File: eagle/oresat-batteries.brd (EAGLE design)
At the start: 99 x 95.3 mm, 107 parts, among them IC1 74AHC1G08DBV, J1 J-SAMTEC-TFM-120-X1-XXX-D-RA, J7 1.27MM-SWD-CONNECTOR, Q1 CSD16340Q3, Q10 TPN4R712MD, Q11 TPN4R712MD, Q12 TPN4R712MD, Q2 CSD16340Q3, Q3 TPN4R712MD, Q4 TPN4R712MD, Q5 TPN4R712MD, Q6 TPN4R712MD, Q8 TPN4R712MD, Q9 TPN4R712MD, U1 TPS63070, U10 LTC4412, U11 MAX17055, U12 LTC4412, U13 LTC4412, U2 TCAN330, U3 BQ2970, U4 LTC4411, U5 LTC4411, U6 STM32F042K6, U7 LTC4411, U8 LTC4411, U9 LTC4412, X1 16MHZ-2.5x2mm

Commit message: New 2S2P battery boards, based on 18650 cells along with a BQ28400 battery IC.
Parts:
- removed C11, C16: 20p, rcl_custom:.0402-B-NOSILK
- removed C14: 22u, oresat-rcl:.0603-B-NOSILK
- removed C17, C22: 100n, rcl_custom:.0402-B-NOSILK
- removed C18, C25: 22u, oresat-rcl:.0805-B-NOSILK
- removed D1, D2, D3: GREEN, SparkFun-LED:LED-0603
- removed F2: 2016L500DR, F-LITTELFUSE-2016L-SERIES-PTC:2016L
- removed H1, H2, H3, H4: STAND-OFFTIGHT, SparkFun-Hardware:STAND-OFF-TIGHT
- removed IC1: 74AHC1G08DBV, 74xx-little-us:SOT23-5
- removed J5: (no value), SparkFun-Connectors:6_PIN_SERIAL_TARGET_SIDE_W_SILK
- removed J7: 1.27MM-SWD-CONNECTOR, J-CNC-3220-10-0100-00-ARM-SWD-port:1.27MM_2X5
- removed JP8: (no value), pinhead:1X02
- removed L3: 1.5 uH, L-Coilcraft-XFL4020:L-COILCRAFT-XFL4020
- removed Q10, Q11, Q12, Q6, Q8, Q9: TPN4R712MD, tpn4r712md-pmosfet:TSON-ADVANCE-3X3
- removed R18: NP, rcl_custom:.0402-B-NOSILK
- removed R19, R21, R26, R28, R29: 10k, rcl:R0603
- removed R20: 4.19, oresat-batteries:RES_HEATER
- removed R22, R23, R24, R25: 470k, rcl:R0603
- removed R27: 3.3k, rcl:R0402
- removed R3: 2.7k, rcl_custom:.0402-B-NOSILK
- removed TP10, TP11, TP12, TP13, TP14, TP16, TP17, TP20, TP6, TP7, TP8, TP9: TP, oresat-batteries:2MM_TP
- removed TP15, TP4, TP5: TEST-POINT, Tova:2MM-TEST-POINT
- removed U$2: (no value), oresat-card:ORESAT-CARD-V1.0
- removed U10, U12, U13, U9: LTC4412, ltc4412:SOT23-6
- removed U11: MAX17055, max17055:TDFN-10L
- removed U2: TCAN330, TCAN330:SOT23-8_TI-DCN
- removed U3: BQ2970, oresat-batteries:PSOP6
- removed U4, U5, U7, U8: LTC4411, ltc4411:SOT23-5-B
- removed U6: STM32F042K6, STM32F042K:QFP32-7X7
- removed X1: 16MHZ-2.5x2mm, low-gain-radio:CRYSTAL_2.5X2
- added B2, B3, B4: B-18650-LI-BATTERY, B-18650-Li-battery:18650
- added TR1: 10k, oresat-rcl:.0603-B-NOSILK
- B1: value 2AHBATT -> B-18650-LI-BATTERY; device oresat-batteries:2AH_605060 -> B-18650-Li-battery:18650
- C1: value .1u -> 1u; device rcl:C0603 -> oresat-rcl:.0603-B-NOSILK
- C10, C7: value .1u -> 100n; device rcl:C0603 -> oresat-rcl:.0402-B-NOSILK
- C2: value .47u -> 100n; device rcl:C0603 -> oresat-rcl:.0402-B-NOSILK
- C3, C5, C9: device rcl_custom:.0402-B-NOSILK -> oresat-rcl:.0402-B-NOSILK
- C4: value 10u -> 100n; device oresat-rcl:.0603-B-NOSILK -> oresat-rcl:.0402-B-NOSILK
- C6: value 10u -> 1u; device oresat-rcl:.0805-B-NOSILK -> oresat-rcl:.0603-B-NOSILK
- C8: value 10u -> 100n; device oresat-rcl:.0805-B-NOSILK -> oresat-rcl:.0402-B-NOSILK
- Q1, Q2: value CSD16340Q3 -> MOSFET-PCH-SOT23-6; device oresat-batteries:Q3 -> Q-MOSFET-PCH-SOT23-6:SOT23-6
- Q3, Q4, Q5: device tpn4r712md-pmosfet:TSON-ADVANCE-3X3 -> Q-Toshiba-TPN4R712MD-MOSFET-P-CH-Power:TSON-ADVANCE-3X3
- R1: value 2.7k -> 10m; device rcl_custom:.0402-B-NOSILK -> oresat-rcl:M2012
- R10: value 470k -> 100; device rcl_custom:.0402-B-NOSILK -> oresat-rcl:1206-B
- R11: value 4.7k -> 3M; device rcl:R0603 -> oresat-rcl:.0603-B-NOSILK
- R12: value 100k -> 3M; device rcl_custom:.0402-B-NOSILK -> oresat-rcl:.0603-B-NOSILK
- R13: value 10k -> 5.1k; device rcl:R0603 -> oresat-rcl:.0603-B-NOSILK
- R14: value 2.2k -> 5.1k; device rcl:R0603 -> oresat-rcl:.0603-B-NOSILK
- R15: value 10k -> 1M; device rcl_custom:.0402-B-NOSILK -> oresat-rcl:.0603-B-NOSILK
- R16: value NP -> 5.1k; device rcl_custom:.0402-B-NOSILK -> oresat-rcl:.0603-B-NOSILK
- R17: value 10k -> 221; device rcl_custom:.0402-B-NOSILK -> oresat-rcl:M2012
- R2: value 2.7k -> 1k; device rcl_custom:.0402-B-NOSILK -> oresat-rcl:.0603-B-NOSILK
- R4: value .01-.05 -> 0? 1k?; device rcl:R2512 -> oresat-rcl:.0603-B-NOSILK
- R5: value 2.2k -> 100; device rcl:R0603 -> oresat-rcl:.0402-B-NOSILK
- R6: value 330 -> 100; device rcl:R0603 -> oresat-rcl:.0402-B-NOSILK
- R7: value 10k -> 1k; device rcl_custom:.0402-B-NOSILK -> oresat-rcl:.0402-B-NOSILK
- R8: value 4.7k -> 1k; device rcl:R0603 -> oresat-rcl:.0402-B-NOSILK
- R9: value DNP/0 -> 100; device rcl:R0603 -> oresat-rcl:1206-B
- U$1: value MMBT3904-TP -> ORESAT-CARD-V0.5; device mmbt3904-tp:SOT23 -> oresat-card:ORESAT-CARD-V1.0
- U1: value TPS63070 -> BQ28400; device ic-pwr-tps63070x:TPS63070X -> U-TI-BQ28400-Li-battery-monitor:TSSOP-20
- moved C9 243.6 mm to (-28.0, -131.0), turned to 0 degrees
- moved TP3 232.2 mm to (-27.0, -144.0), turned to 0 degrees
- moved R17 228.7 mm to (-28.0, -126.0)
- moved TP2 223.6 mm to (-27.0, -140.0), turned to 0 degrees
- moved F1 217.8 mm to (-26.8, -147.4)
- moved R16 212.1 mm to (-28.0, -121.0), turned to 0 degrees
- moved R15 202.6 mm to (-28.0, -116.0), turned to 0 degrees
- moved R12 192.0 mm to (-28.0, -101.0), turned to 0 degrees
- moved TP1 178.7 mm to (-6.00, -93.0), turned to 0 degrees
- moved C8 171.1 mm to (-7.00, -88.0), turned to 0 degrees
- moved R10 167.8 mm to (-6.00, -83.0), turned to 0 degrees
- moved R7 148.7 mm to (-7.00, -64.0), turned to 0 degrees
- moved C3 141.7 mm to (-7.00, -37.0)
- moved C6 137.4 mm to (-7.00, -50.0), turned to 0 degrees
- moved C5 129.8 mm to (-7.00, -43.0), turned to 0 degrees
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- renumbered J1 to J6
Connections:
- net SPARE10 renamed CAN1_L
- net SPARE12 renamed !SHUTDOWN
- net SPARE9 renamed CAN1_H
- removed net !SYSSHD: IC1.1, J6.7, J6.8, R14.2, TP8.P$1
- removed net .3556: Q4.5, Q4.6, Q4.7, Q4.8, Q9.5, Q9.6, Q9.7, Q9.8, U10.6, U13.1
- removed net 3.3V: C14.1, C17.2, C18.1, C22.2, C25.1, C3.2, C9.2, J7.VTREF, R10.2, R11.2, R13.2, R16.2, R2.2, R22.1, R23.1, R24.1, R25.1, R8.2, TP1.1, U1.7-8, U2.3, U6.1, U6.17, U6.5
- removed net 4411MB: U7.5, U8.1
- removed net 4411_MT: U4.5, U5.1
- removed net ALERT: R13.1, R9.2, TP17.P$1, U11.8
- removed net ANDDRIVE: IC1.4, Q1.P$4
- removed net BATT-: B1.NEG, IC1.3, Q1.P$1, Q1.P$2, Q1.P$3, TP20.P$1, U3.4
- removed net BETSHUT: Q1.P$5, Q1.P$6, Q1.P$7, Q1.P$8, Q1.P$9, Q2.P$5, Q2.P$6, Q2.P$7, Q2.P$8, Q2.P$9
- removed net BGDOUT: IC1.2, TP10.P$1, U3.3
- removed net BOOT: R17.2, TP15.1, U6.31
- removed net BQBAT: C1.1, R6.1, TP6.P$1, U3.5
- removed net BQCOUT: Q2.P$4, TP9.P$1, U3.2
- removed net BQVMIN: R5.1, U3.6
- removed net CAN_H: J6.3, J6.4, U2.7
- removed net CAN_L: J6.1, J6.2, U2.6
- removed net CAN_RX: U2.4, U6.21
- removed net CAN_SHDN: U2.5, U6.20
- removed net CAN_SILENT: U2.8, U6.19
- removed net CAN_TX: U2.1, U6.22
- removed net CHARGE-STAT-U4-U5: R25.2, U4.4, U5.4, U6.11
- removed net CHARGE-STAT-U7-U8: R24.2, U6.10, U7.4, U8.4
- removed net CHARGE_ENABLE: R29.2, TP11.P$1, U4.3, U5.3, U6.15, U7.3, U8.3
- removed net CRYSTALIN: C16.1, U6.2, X1.1
- removed net CRYSTALOUT: C11.1, U6.3, X1.3
- removed net C_SENSE: Q2.P$1, Q2.P$2, Q2.P$3, R21.1, R4.2, R5.2, TP13.P$1, U11.6
- removed net DISCHARGE-STAT-U10-U13: R23.2, U12.4, U6.13, U9.4
- removed net DISCHARGE-STAT-U9-U12: R22.2, U10.4, U13.4, U6.12
- removed net DISCHARGE_ENABLE: R26.1, TP14.P$1, U10.3, U12.3, U13.3, U6.26, U9.3
- removed net HEAT: R27.1, U6.14
- removed net HEAT_FET_CTL: Q12.4, R28.1, U$1.3
- removed net INFUSE: F1.1, U4.1, U7.1
- removed net MAX_IO: R9.1, U6.7
- removed net N$1: D3.A, R3.1
- removed net N$2: Q3.1, Q3.2, Q3.3, Q8.1, Q8.2, Q8.3
- removed net N$270: D1.A, R1.1
- removed net N$271: D2.A, R2.1
- removed net N$3: Q10.1, Q10.2, Q10.3, Q5.1, Q5.2, Q5.3
- removed net N$4: Q11.1, Q11.2, Q11.3, Q4.1, Q4.2, Q4.3
- removed net N$406: J5.P$4, JP8.2
- removed net N$436: Q10.4, Q5.4, U12.5
- removed net N$437: Q10.5, Q10.6, Q10.7, Q10.8, Q3.5, Q3.6, Q3.7, Q3.8, U12.1, U9.6
- removed net N$438: Q3.4, Q8.4, U9.5
- removed net N$439: Q6.4, Q9.4, U13.5
- removed net N$441: Q11.4, Q4.4, U10.5
- removed net N$5: Q6.1, Q6.2, Q6.3, Q9.1, Q9.2, Q9.3
- removed net N$6: Q12.5, Q12.6, Q12.7, Q12.8, R20.V+
- removed net N$7: R27.2, U$1.1
- removed net NRESET: J7.!RESET, U6.4
- removed net OUTFUSE: F2.2, Q5.5, Q5.6, Q5.7, Q5.8, Q6.5, Q6.6, Q6.7, Q6.8, U12.6, U13.6
- removed net PA0: R3.2, U6.6
- removed net PA2/USART2_TX: J5.P$2, U6.8
- removed net PA3/USART2_RX: J5.P$3, U6.9
- removed net REG: C2.1, U11.7
- removed net SCL: R11.1, TP7.P$1, U11.3, U6.29
- removed net SDA: R8.1, TP16.P$1, U11.4, U6.30
- removed net SPARE11: J6.37, J6.38
- removed net SPARE8: J6.31, J6.32
- removed net SWCLK: J7.SWDCLK, U6.24
- removed net SWDIO: J7.SWDIO, U6.23
- removed net TEMPSENSE: R19.1, R21.2, U11.2
- removed net THRM: R19.2, U11.9
- removed net TPS-EN1: R18.2, R7.1, TP5.1, U1.1, U1.14
- removed net TPS-FB1: R10.1, R12.2, U1.5
- removed net TPS-FB3: TP3.1, U1.6
- removed net TPS-L3: L3.1, U1.11
- removed net TPS-L4: L3.2, U1.9
- removed net TPS-PG1: R16.1, TP2.1, U1.2
- removed net TPS-VAUX1: C5.1, U1.3
- removed net TPS-VSEL1: R15.2, TP4.1, U1.15
- removed net V_BATT: B1.POS, C10.1, C7.1, IC1.5, Q11.5, Q11.6, Q11.7, Q11.8, Q12.1, Q12.2, Q12.3, Q8.5, Q8.6, Q8.7, Q8.8, R14.1, R28.2, R6.2, TP12.P$1, U10.1, U11.10, U5.5, U8.5, U9.1
- new net !CB_EN: TP1.1, U1.9
- new net !PRES: R2.1, U1.13
- new net BQ-SCLK: TP3.1, U1.12
- new net BQ-SDA: TP2.1, U1.10
- new net CAN2_H: J6.21, J6.22
- new net CAN2_L: J6.23, J6.24
- new net CHG: R13.2, U1.19
- new net DSG: R14.2, U1.2
- new net FUSE: R4.1, U1.17
- new net GNDA: B3.NEG, B4.NEG, C1.2, C2.2, C3.2, C4.2, C6.2, C7.2, C8.2, R1.2, R2.2, R4.2, R6.1, R9.1, TR1.1, U1.15, U1.5
- new net N$10: Q1.1, Q1.2, Q1.5, Q1.6, R9.2
- new net N$11: Q2.1, Q2.2, Q2.5, Q2.6, R10.2
- new net N$13: Q3.5, Q3.6, Q3.7, Q3.8, Q4.5, Q4.6, Q4.7, Q4.8, R17.2
- new net N$14: Q3.4, R11.2, R13.1
- new net N$15: Q4.4, R12.2, R14.1
- new net N$18: Q5.4, R15.2, R16.1
- new net N$20: Q5.5, Q5.6, Q5.7, Q5.8, R17.1
- new net N$21: C10.1, C9.2
- new net OPD_PWR: J6.19, J6.20
- new net OPD_SCL: J6.17, J6.18
- new net OPD_SDA: J6.15, J6.16
- new net PACK: C9.1, F1.1, Q3.1, Q3.2, Q3.3, Q5.1, Q5.2, Q5.3, R11.1, R15.1, U1.20
- new net RBI: C2.1, U1.14
- new net REG27: C1.1, U1.16
- new net SRN: C3.1, C5.1, R5.2, U1.7
- new net SRP: C4.1, C5.2, R6.2, U1.6
- new net TS1: TR1.2, U1.8
- new net V1S: B1.NEG, B2.NEG, B3.POS, B4.POS, Q1.4, R10.1, R8.2
- new net V2S: B1.POS, B2.POS, C10.2, C6.1, Q2.4, Q4.1, Q4.2, Q4.3, R12.1, R7.2, U1.1
- new net VC1: C8.1, Q2.3, R7.1, U1.3
- new net VC2: C7.1, Q1.3, R8.1, U1.4
- new net ZVCHG: R16.2, U1.18
- net GND: now also J6.29, J6.30, J6.31, J6.32, J6.37, J6.38, R1.1, R5.1; no longer C1.2, C10.2, C11.2, C14.2, C16.2, C17.1, C18.2, C2.2, C22.1, C25.2, C3.1, C4.2, C5.2, C6.2, C7.2, C8.2, C9.1, D1.C, D2.C, D3.C, J5.P$6, J6.10, J6.11, J6.12, J6.5, J6.6, J6.9, J7.GND, J7.GND@2, J7.GNDDET, R12.1, R15.1, R17.1, R18.1, R20.V-, R26.2, R29.1, R4.1, U$1.2, U1.10, U1.4, U10.2, U11.5, U12.2, U13.2, U2.2, U4.2, U5.2, U6.16, U6.32, U7.2, U8.2, U9.2, X1.2, X1.4
- net SPARE1: now also J6.13, J6.14; no longer J6.17, J6.18
- net SPARE2: now also J6.11, J6.12; no longer J6.19, J6.20
- net SPARE3: now also J6.10, J6.9; no longer J6.21, J6.22
- net SPARE4: now also J6.7, J6.8; no longer J6.23, J6.24
- net SPARE5: now also J6.5, J6.6; no longer J6.25, J6.26
- net SPARE6: now also J6.3, J6.4; no longer J6.27, J6.28
- net SPARE7: now also J6.1, J6.2; no longer J6.29, J6.30
- net VBUS: now also J6.25, J6.26, J6.27, J6.28; no longer C4.1, C6.1, C8.1, F2.1, J6.13, J6.14, J6.15, J6.16, JP8.1, R1.2, R7.2, U1.12-13
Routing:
- net CAN_H: track 109.3 -> 0.00 mm, vias 2 -> 0
- net CAN_L: track 109.1 -> 0.00 mm, vias 3 -> 0
- net NRESET: track 98.8 -> 0.00 mm, vias 2 -> 0
- net SWCLK: track 95.1 -> 0.00 mm, vias 4 -> 0
- net SWDIO: track 85.8 -> 0.00 mm, vias 2 -> 0
- net PA0: track 77.4 -> 0.00 mm, vias 2 -> 0
- net 3.3V: track 71.7 -> 0.00 mm, vias 1 -> 0
- net PA2/USART2_TX: track 42.2 -> 0.00 mm, vias 1 -> 0
- net PA3/USART2_RX: track 41.5 -> 0.00 mm
- net CHARGE_ENABLE: track 31.0 -> 0.00 mm
- net HEAT: track 27.9 -> 0.00 mm
- net DISCHARGE-STAT-U10-U13: track 24.7 -> 0.00 mm
- net DISCHARGE-STAT-U9-U12: track 21.5 -> 0.00 mm
- net SCL: track 20.0 -> 0.00 mm
- net CHARGE-STAT-U4-U5: track 18.3 -> 0.00 mm
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- added copper zone on layer 1, net GNDA
- added copper zone on layer 1, net V1S
- added copper zone on layer 1, net V2S
- removed copper zone on layer 1, net 3.3V
- removed copper zone on layer 1, net BOOT
- removed copper zone on layer 1, net TPS-L3
- removed copper zone on layer 1, net TPS-L4
- removed copper zone on layer 1, net VBUS
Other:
- board text added: "+"
- board text added: "-"
- board text removed: "2018/03/12"
- board text removed: "3.3V"
- board text removed: "GND"
- board text removed: "OreSat Proto-Card v2.0"
- board text removed: "PA0"
- board text removed: "PA1"
- board text removed: "PA15"
- board text removed: "PA2/TX"
- board text removed: "PA3/RX"
- board text removed: "PA4"
- board text removed: "PA5"
- board text removed: "PA6"
- board text removed: "PA7"
- board text removed: "PA8"
- board text removed: "PB0"
- board text removed: "PB1"
- board text removed: "PB3"
- board text removed: "PB4"
- board text removed: "PB5"
- board text removed: "PB6/CL"
- board text removed: "PB7/SD"
- board text removed: "PSAS"
- board text removed: "VBAT"
- board text removed: "VBUS to VUSB"

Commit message: update schematic with s8209 and MAX17205 chips for battery protection and control
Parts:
- removed F1: 2016L200PR, F-LITTELFUSE-2016L-SERIES-PTC:2016L
- removed TR1: 10k, oresat-rcl:.0603-B-NOSILK
- added C11, C16: 20p, rcl_custom:.0402-B-NOSILK
- added C12: 22u, oresat-rcl:.0805-B-NOSILK
- added C13, C15: 1n, oresat-rcl:C0402
- added C14: .1u, oresat-rcl:C0402
- added C17, C22: 100n, rcl_custom:.0402-B-NOSILK
- added C18: 10n, rcl:C0402K
- added C19, C21: 100n, rcl:C0402K
- added D1, D2: GREEN, SparkFun-LED:LED-0603
- added D4: AMBER, SparkFun-LED:LED-0603
- added J1: J-SAMTEC-TFM-110-X1-XXX-D-RA, J-Samtec-TFM-110-X1-XXX-D-RA:J-SAMTEC-TFM-110-X1-XXX-D-RA
- added L2: 6.8u, L-ECS-MPI4040:ECS-MPI4040
- added Q6: PMV45EN, Tova:SOT23
- added R18, R26, R27, R28, R30, R35, R38: 10k, rcl_custom:.0402-B-NOSILK
- added R19, R20, R21, R22, R23, R32, R34, R36, R37: NP, rcl_custom:.0402-B-NOSILK
- added R24, R25: 100, rcl_custom:.0402-B-NOSILK
- added R29: 100m, rcl:R1206
- added R3, R46, R49, R50: 4.7k, rcl:R0402
- added R31, R33: 0, rcl_custom:.0402-B-NOSILK
- added R39: 10, oresat-rcl:.0603-B
- added R40: .01, rcl:R0805
- added R41, R42: 10k, rcl:R0603
- added R43, R44: 10k, oresat-rcl:R0603
- added R47, R48, R51, R52: 1k, rcl:R0402
- added R53, R54: 470, rcl:R0402
- added R55: 100, rcl:R0603
- added TP10, TP11, TP12, TP13, TP14, TP15, TP16, TP17, TP18, TP19, TP20, TP4, TP5, TP6, TP8, TP9: TEST-POINT, Tova:2MM-TEST-POINT
- added U$3, U$4: S8209A, U-ABLIC-s8209A-BattProtection:TSSOP8
- added U2: TCAN330, TCAN330:SOT23-8_TI-DCN
- added U3: MAX7310ATE, U-Maxim-MAX7310-I2C-GPIO-expander:QFN65P400X400X80-17T210
- added U4: MAX4211CETE, U-Maxim-MAX4211-power-monitor:QFN65P400X400X80-17T210
- added U5: TPS62111RSA, U-TI-TPS6211x-SPS-buck:S-PVQFN-16
- added U6: STM32F042K6, STM32F042K:QFP32-7X7
- added U7: MCP1703A, v-reg:SOT23
- added X1: 16MHZ-2.5x2mm, low-gain-radio:CRYSTAL_2.5X2
- C1: value 1u -> 100n; device oresat-rcl:.0603-B-NOSILK -> rcl_custom:.0402-B-NOSILK
- C10, C4, C5: value 100n -> 1u; device oresat-rcl:.0402-B-NOSILK -> oresat-rcl:.0603-B-NOSILK
- C2: value 100n -> NP; device oresat-rcl:.0402-B-NOSILK -> rcl_custom:.0402-B-NOSILK
- C3, C9: device oresat-rcl:.0402-B-NOSILK -> rcl_custom:.0402-B-NOSILK
- C6: value 1u -> TBD; device oresat-rcl:.0603-B-NOSILK -> rcl_custom:.0402-B-NOSILK
- C7: value 100n -> 10u; device oresat-rcl:.0402-B-NOSILK -> oresat-rcl:.0805-B-NOSILK
- C8: value 100n -> TBD; device oresat-rcl:.0402-B-NOSILK -> rcl_custom:.0402-B-NOSILK
- Q1: value MOSFET-PCH-SOT23-6 -> DMP2240UDM; device Q-MOSFET-PCH-SOT23-6:SOT23-6 -> Q-MOSFET-PCH-dual-SOT23-6:SOT23-6
- Q2: device Q-MOSFET-PCH-SOT23-6:SOT23-6 -> Q-MOSFET-PCH-dual-SOT23-6:SOT23-6
- Q3, Q4: value TPN4R712MD -> MOSFET-PCH-SOT23-6; device Q-Toshiba-TPN4R712MD-MOSFET-P-CH-Power:TSON-ADVANCE-3X3 -> Q-MOSFET-PCH-SOT23-6:SOT23-6
- Q5: value TPN4R712MD -> PMV45EN; device Q-Toshiba-TPN4R712MD-MOSFET-P-CH-Power:TSON-ADVANCE-3X3 -> Tova:SOT23
- R1: value 10m -> 2.7k; device oresat-rcl:M2012 -> rcl_custom:.0402-B-NOSILK
- R10, R9: value 100 -> NP; device oresat-rcl:1206-B -> rcl_custom:.0402-B-NOSILK
- R11: value 3M -> NP; device oresat-rcl:.0603-B-NOSILK -> rcl_custom:.0402-B-NOSILK
- R12: value 3M -> 2.7k; device oresat-rcl:.0603-B-NOSILK -> rcl_custom:.0402-B-NOSILK
- R13, R14: value 5.1k -> NP; device oresat-rcl:.0603-B-NOSILK -> rcl_custom:.0402-B-NOSILK
- R15: value 1M -> 10k; device oresat-rcl:.0603-B-NOSILK -> rcl_custom:.0402-B-NOSILK
- R16: value 5.1k -> 10k; device oresat-rcl:.0603-B-NOSILK -> rcl_custom:.0402-B-NOSILK
- R17: value 221 -> 10k; device oresat-rcl:M2012 -> rcl_custom:.0402-B-NOSILK
- R2: value 1k -> 2.7k; device oresat-rcl:.0603-B-NOSILK -> rcl_custom:.0402-B-NOSILK
- R4: value 0? 1k? -> 100; device oresat-rcl:.0603-B-NOSILK -> rcl_custom:.0402-B-NOSILK
- R5, R6: value 100 -> NP; device oresat-rcl:.0402-B-NOSILK -> rcl_custom:.0402-B-NOSILK
- R7: value 1k -> 10k; device oresat-rcl:.0402-B-NOSILK -> rcl_custom:.0402-B-NOSILK
- R8: value 1k -> NP; device oresat-rcl:.0402-B-NOSILK -> rcl_custom:.0402-B-NOSILK
- U$1: value ORESAT-CARD-V0.5 -> ORESAT-CARD-V1.1-3XRF; device oresat-card:ORESAT-CARD-V1.0 -> oresat-cards:ORESAT-CARD-V1.1-3XRF
- U1: value BQ28400 -> MAX17205G; device U-TI-BQ28400-Li-battery-monitor:TSSOP-20 -> U-Maxim-MAX17205-Fuel_Gauge:21-0137I_T1433-2
- moved TP3 221.5 mm to (52.8, 62.6)
- moved C9 221.1 mm to (11.9, 86.5), turned to 180 degrees
- moved TP2 219.4 mm to (52.8, 64.4)
- moved C10 212.9 mm to (28.2, 70.3), turned to 180 degrees
- moved R17 207.9 mm to (2.00, 79.7), turned to 90 degrees
- moved R16 207.4 mm to (64.7, 64.5)
- moved R15 202.4 mm to (67.0, 62.7)
- moved R14 201.1 mm to (55.2, 72.1)
- moved R13 197.4 mm to (57.2, 72.1), turned to 180 degrees
- moved R11 186.7 mm to (55.2, 71.1), turned to 180 degrees
- moved R12 185.1 mm to (60.0, 61.9), turned to 180 degrees
- moved Q5 176.7 mm to (47.8, 70.1), turned to 90 degrees
- moved Q4 174.3 mm to (44.0, 72.1)
- moved TP1 172.4 mm to (60.6, 66.0)
- moved C8 167.7 mm to (64.7, 63.6)
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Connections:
- net CAN2_H renamed N$525
- net CAN2_L renamed N$524
- net SPARE1 renamed N$528
- net SPARE2 renamed N$500
- net SPARE3 renamed N$503
- net SPARE5 renamed N$504
- net SPARE6 renamed N$519
- net SPARE7 renamed N$520
- removed net !CB_EN: TP1.1, U1.9
- removed net !PRES: R2.1, U1.13
- removed net BQ-SCLK: TP3.1, U1.12
- removed net BQ-SDA: TP2.1, U1.10
- removed net CHG: R13.2, U1.19
- removed net DSG: R14.2, U1.2
- removed net FUSE: R4.1, U1.17
- removed net GNDA: B3.NEG, B4.NEG, C1.2, C2.2, C3.2, C4.2, C6.2, C7.2, C8.2, R1.2, R2.2, R4.2, R6.1, R9.1, TR1.1, U1.15, U1.5
- removed net N$13: Q3.5, Q3.6, Q3.7, Q3.8, Q4.5, Q4.6, Q4.7, Q4.8, R17.2
- removed net N$18: Q5.4, R15.2, R16.1
- removed net N$20: Q5.5, Q5.6, Q5.7, Q5.8, R17.1
- removed net N$21: C10.1, C9.2
- removed net PACK: C9.1, F1.1, Q3.1, Q3.2, Q3.3, Q5.1, Q5.2, Q5.3, R11.1, R15.1, U1.20
- removed net RBI: C2.1, U1.14
- removed net REG27: C1.1, U1.16
- removed net SRN: C3.1, C5.1, R5.2, U1.7
- removed net SRP: C4.1, C5.2, R6.2, U1.6
- removed net TS1: TR1.2, U1.8
- removed net V2S: B1.POS, B2.POS, C10.2, C6.1, Q2.4, Q4.1, Q4.2, Q4.3, R12.1, R7.2, U1.1
- removed net VC1: C8.1, Q2.3, R7.1, U1.3
- removed net VC2: C7.1, Q1.3, R8.1, U1.4
- removed net ZVCHG: R16.2, U1.18
- new net !FAULT: Q6.3, R38.1, TP8.1, U3.7
- new net 3.3V: C12.1, C17.2, C22.2, C3.2, C9.2, L2.2, R2.2, TP17.1, U2.3, U5.10, U6.1, U6.17, U6.5
- new net AD0: R5.1, R6.2, R8.2, R9.1, U3.1
- new net AD1: R11.1, R13.2, R14.2, R19.1, U3.2
- new net AD2: R20.1, R21.2, R22.2, R23.1, U3.3
- new net AUX_!SHUTDOWN: J1.19, J1.20
- new net AUX_CAN1_H: J1.13, J1.14
- new net AUX_CAN1_L: J1.15, J1.16
- new net AUX_CAN2_H: J1.1, J1.2
- new net AUX_CAN2_L: J1.3, J1.4
- new net AUX_GND1: J1.17, J1.18
- new net AUX_GND2: J1.11, J1.12
- new net AUX_GND3: J1.10, J1.9
- new net AUX_VBUS1: J1.7, J1.8
- new net AUX_VBUS2: J1.5, J1.6
- new net BOOT: R17.2, TP15.1, U6.31
- new net CAN_RX: U2.4, U6.21
- new net CAN_SHDN: U2.5, U6.20
- new net CAN_SILENT: U2.8, U6.19
- new net CAN_TX: U2.1, U6.22
- new net CB-RESET: R30.2, TP14.1, U3.5, U4.8
- new net CB_CTRL: Q3.3, Q6.1, R35.1, U4.3, U4.4, U4.6
- new net CRYSTALIN: C16.1, U6.2, X1.1
- new net CRYSTALOUT: C11.1, U6.3, X1.3
- new net MAX4211-3V3: C5.1, U4.1, U7.2
- new net N$1: R3.2, R46.2
- new net N$12: C18.1, U$3.4
- new net N$16: R53.1, U$3.3
- new net N$17: R54.1, U$4.3
- new net N$2: R47.2, U$3.2
- new net N$270: D1.A, R1.1
- new net N$271: D2.A, R2.1
- new net N$3: R47.1, U$4.6
- new net N$385: C13.1, C14.1, R39.1, U1.5
- new net N$398: C4.1, Q3.4, R29.2, R35.2, U4.15, U7.3
- new net N$4: R48.2, U$3.1
- new net N$401: R41.2, R42.2, U1.14
- new net N$403: R41.1, R43.2, U1.10
- new net N$404: R42.1, R44.2, U1.9
- new net N$405: U1.8
- new net N$407: B3.NEG, B4.NEG, C15.2, C19.2, R40.1, R51.1, R52.1, U$4.5, U1.2
- new net N$480: TP2.1, U3.8
- new net N$482: TP3.1, U3.9
- new net N$499: C13.2, C15.1, R55.2, U1.6, U1.7
- new net N$5: R51.2, U$4.4
- new net N$518: TP4.1, U3.10
- new net N$523: TP5.1, U3.11
- new net N$573: R12.2, TP10.1, U3.12
- new net N$575: D4.A, R12.1
- new net N$579: C6.1, Q1.5, R25.2
- new net N$580: C6.2, Q1.1, Q1.4, R15.2
- new net N$581: C8.2, Q1.3, R16.2, R18.1
- new net N$589: R26.1, U3.13
- new net N$590: Q4.3, Q5.3, R27.1
- new net N$593: Q4.1, Q4.2, Q4.5, Q4.6, R29.1, U4.16
- new net N$596: R31.1, R32.2, TP12.1, U4.10
- new net N$597: R33.1, R34.2, TP11.1, U4.11
- new net N$598: R31.2, U4.14
- new net N$599: R33.2, U4.12, U4.9
- new net N$6: R48.1, U$4.7
- new net N$600: TP6.1, U4.13
- new net N$603: C2.1, R36.2, R37.2
- new net N$604: R37.1, U4.5
- new net N$8: Q2.1, R50.1, U$3.6
- new net N$9: Q2.3, R49.1, U$3.7
- new net ON/!OFF: Q5.1, R28.2, TP13.1, U3.4
- new net PEN-SCL-FILT: R13.1, R21.1, R24.2, R6.1, TP18.1, U3.15
- new net PEN-SDA-FILT: Q1.6, R16.1, R19.2, R23.2, R9.2, TP20.1, U3.16
- new net SCL: R3.1, U1.11, U6.29
- new net SDA: R46.1, U1.12, U6.30
- new net TPS62111-PG: TP16.1, U5.13
- new net TPS62111-SYNC: R10.2, R7.1, TP19.1, U5.5
- new net TPS62111_SW: L2.1, U5.14, U5.15
- new net VBUSP: C10.1, C2.2, C7.1, Q3.1, Q3.2, Q3.5, Q3.6, R1.2, R7.2, TP9.1, U5.2, U5.3, U5.4, U5.8
- new net VPD: C1.2, C8.1, Q1.2, R11.2, R18.2, R20.2, R26.2, R38.2, R4.2, R5.2, TP1.1, U3.14
- net CAN1_H: now also U2.7
- net CAN1_L: now also U2.6
- net GND: now also C1.1, C10.2, C11.2, C12.2, C14.2, C16.2, C17.1, C22.1, C3.1, C4.2, C5.2, C7.2, C9.1, D1.C, D2.C, D4.C, Q5.2, Q6.2, R10.1, R14.1, R15.1, R17.1, R22.1, R28.1, R30.1, R32.1, R34.1, R36.1, R40.2, R43.1, R44.1, R8.1, U1.13, U1.15, U1.4, U2.2, U3.6, U3.EPAD, U4.7, U4.EPAD, U5.1, U5.11, U5.12, U5.16, U5.6, U5.7, U5.9, U5.PAD, U6.16, U6.32, U7.1, X1.2, X1.4; no longer R1.1, R5.1
- net N$10: now also Q2.5, R39.2, R50.2; no longer Q1.1, Q1.2, Q1.5, Q1.6, R9.2
- net N$11: now also Q2.4; no longer Q2.1, Q2.2, Q2.5, R10.2
- net N$14: now also R52.2, U$4.2; no longer Q3.4, R11.2, R13.1
- net N$15: now also B1.POS, B2.POS, C21.1, Q2.2, R49.2, R53.2; no longer Q4.4, R12.2, R14.1
- net OPD_PWR: now also R4.1
- net OPD_SCL: now also R24.1
- net OPD_SDA: now also R25.1
- net V1S: now also C18.2, C19.1, C21.2, R54.2, R55.1, U$3.5; no longer Q1.4, R10.1, R8.2
- net VBUS: now also Q4.4, R27.2; no longer F1.2
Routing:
- net OPD_PWR: track 0.00 -> 49.4 mm
- net 3.3V: track 0.00 -> 49.1 mm
- net VPD: track 0.00 -> 47.9 mm, vias 0 -> 6
- net OPD_SCL: track 0.00 -> 42.6 mm
- net OPD_SDA: track 0.00 -> 39.5 mm
- net CAN_SHDN: track 0.00 -> 34.3 mm, vias 0 -> 2
- net CAN_RX: track 0.00 -> 33.8 mm, vias 0 -> 2
- net PEN-SDA-FILT: track 0.00 -> 32.2 mm, vias 0 -> 4
- net CAN_SILENT: track 0.00 -> 32.1 mm, vias 0 -> 2
- net CB_CTRL: track 0.00 -> 30.4 mm, vias 0 -> 3
- net CAN_TX: track 0.00 -> 30.2 mm, vias 0 -> 2
- net PEN-SCL-FILT: track 0.00 -> 25.7 mm, vias 0 -> 4
- net CAN1_L: track 0.00 -> 24.7 mm, vias 0 -> 1
- net N$398: track 0.00 -> 18.6 mm, vias 0 -> 2
- net CB-RESET: track 0.00 -> 15.1 mm, vias 0 -> 1
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- added copper zone on layer 1, net 3.3V
- added copper zone on layer 1, net N$398
- added copper zone on layer 1, net N$593
- added copper zone on layer 1, net TPS62111_SW
- added copper zone on layer 1, net VBUS
- added copper zone on layer 1, net VBUSP
- removed copper zone on layer 1, net GNDA
- removed copper zone on layer 1, net V1S
- removed copper zone on layer 1, net V2S
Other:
- board size 99 x 95.3 mm -> 99.8 x 94.7 mm
- board text added: "1"
- board text added: "10"
- board text added: "2"
- board text added: "2019/07/27"
- board text added: "3"
- board text added: "4"
- board text added: "5"
- board text added: "6"
- board text added: "7"
- board text added: "8"
- board text added: "9"
- board text added: "C2H"
- board text added: "C2L"
- board text added: "OreSat Battery Card 1.0"
- board text added: "PA0"
- board text removed: "+"
- board text removed: "-"

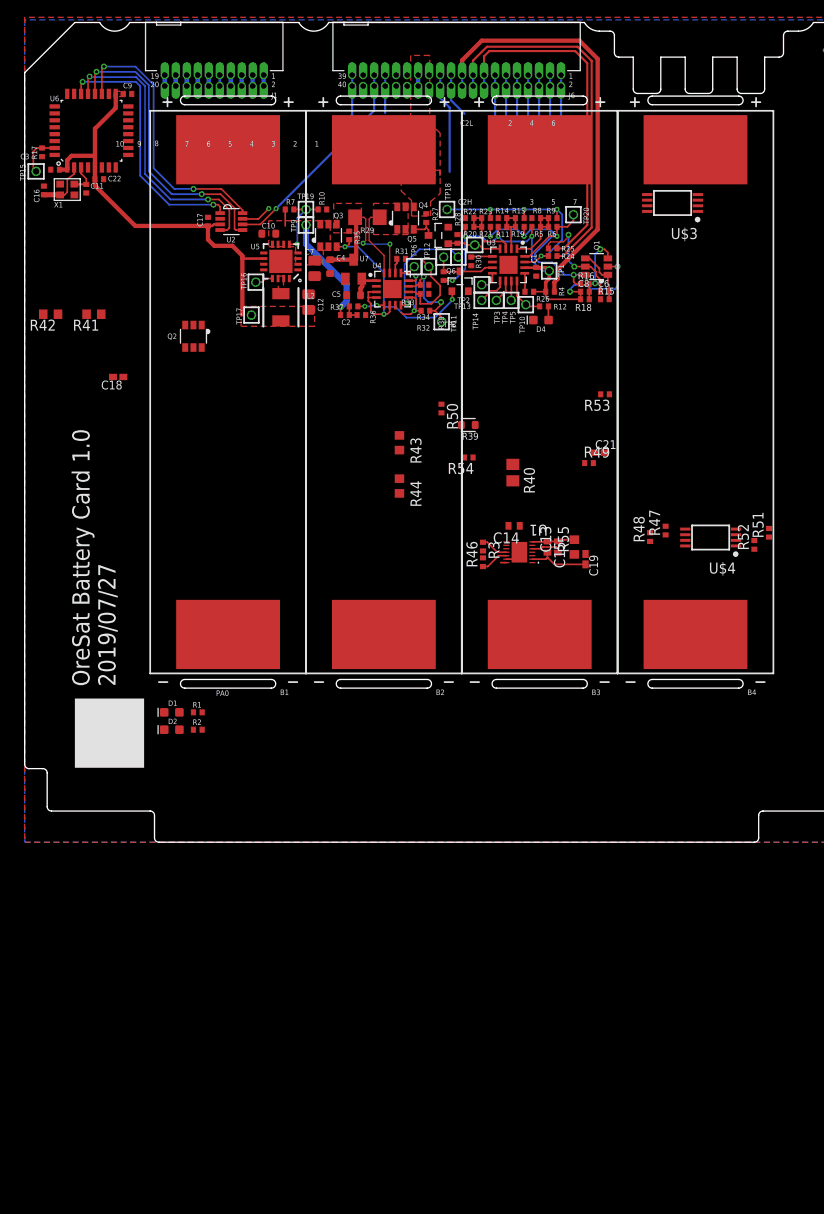
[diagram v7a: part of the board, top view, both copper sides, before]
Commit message: Design review of schematic. Added labels, nets to M0, shutdown circuitry, discussed power domains.
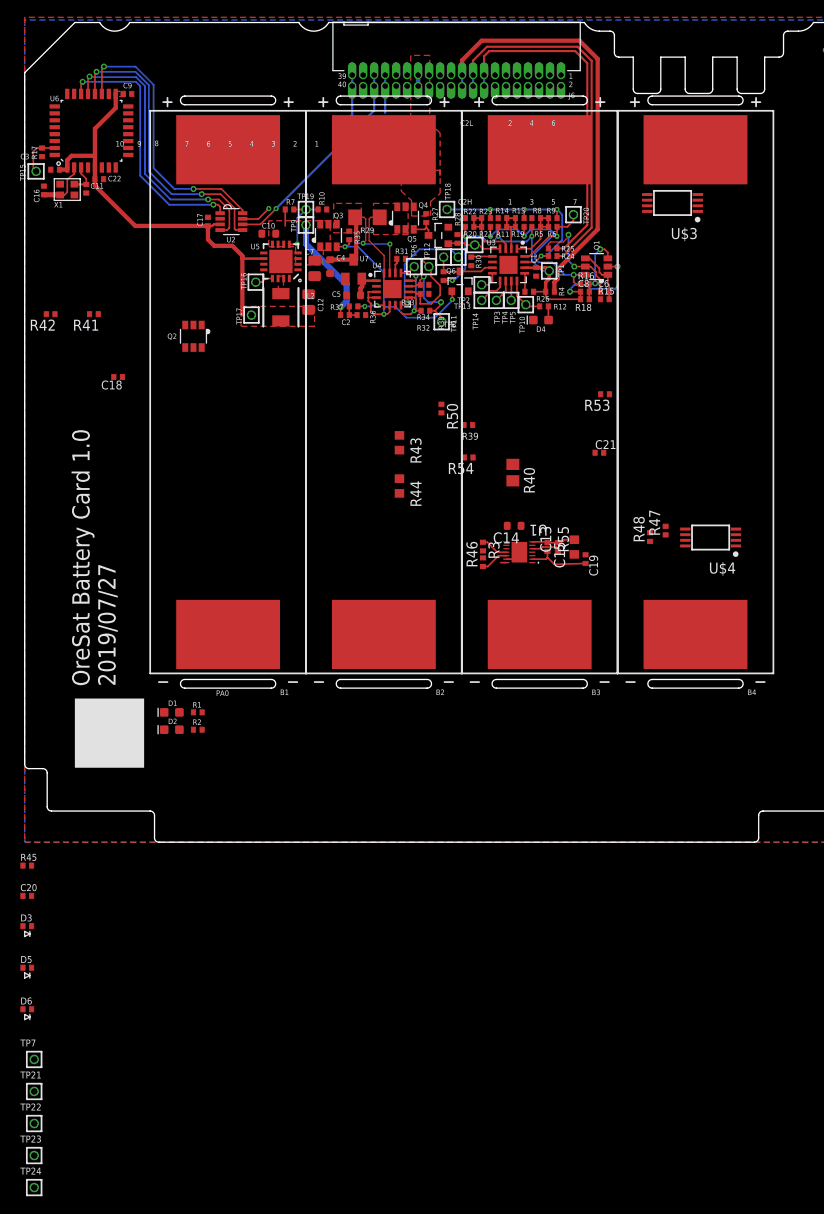
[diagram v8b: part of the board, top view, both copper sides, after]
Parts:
- removed J1: J-SAMTEC-TFM-110-X1-XXX-D-RA, J-Samtec-TFM-110-X1-XXX-D-RA:J-SAMTEC-TFM-110-X1-XXX-D-RA
- removed R49: 4.7k, rcl:R0402
- removed R51, R52: 1k, rcl:R0402
- added C20: 10n, rcl_custom:.0402-B-NOSILK
- added D3, D5, D6: D-0402, D-0402-package:.0402-B-NOSILK-DIODE
- added R45: 100k, rcl_custom:.0402-B-NOSILK
- added TP21, TP22, TP23, TP24, TP7: TEST-POINT, Tova:2MM-TEST-POINT
- C13, C15: device oresat-rcl:C0402 -> rcl_custom:.0402-B-NOSILK
- C14: device oresat-rcl:C0402 -> rcl_custom:.0603-B-NOSILK
- C18, C19, C21: device rcl:C0402K -> rcl_custom:.0402-B-NOSILK
- R39: device oresat-rcl:.0603-B -> rcl_custom:.0402-B-NOSILK
- R41, R42: device rcl:R0603 -> rcl_custom:.0402-B-NOSILK
- R47, R48, R53, R54: device rcl:R0402 -> rcl_custom:.0402-B-NOSILK
- R50: value 4.7k -> 100k; device rcl:R0402 -> rcl_custom:.0402-B-NOSILK
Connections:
- removed net AUX_!SHUTDOWN: J1.19, J1.20
- removed net AUX_CAN1_H: J1.13, J1.14
- removed net AUX_CAN1_L: J1.15, J1.16
- removed net AUX_CAN2_H: J1.1, J1.2
- removed net AUX_CAN2_L: J1.3, J1.4
- removed net AUX_GND1: J1.17, J1.18
- removed net AUX_GND2: J1.11, J1.12
- removed net AUX_GND3: J1.10, J1.9
- removed net AUX_VBUS1: J1.7, J1.8
- removed net AUX_VBUS2: J1.5, J1.6
- removed net N$1: R3.2, R46.2
- removed net N$10: Q2.5, R39.2, R50.2
- removed net N$500: J6.11, J6.12
- removed net N$503: J6.10, J6.9
- removed net N$504: J6.5, J6.6
- removed net N$519: J6.3, J6.4
- removed net N$520: J6.1, J6.2
- removed net N$524: J6.23, J6.24
- removed net N$525: J6.21, J6.22
- removed net N$528: J6.13, J6.14
- removed net SPARE4: J6.7, J6.8
- new net !CHRG-DISABLE: D6.C
- new net !SHDWN-M0: D3.C
- new net N$7: C20.1, U$4.4
- net !SHUTDOWN: now also D5.C
- net 3.3V: now also R3.2, R46.2
- net N$14: now also D6.A, TP22.1, U$4.1; no longer R52.2, U$4.2
- net N$15: now also R45.2; no longer R49.2
- net N$2: now also TP24.1
- net N$4: now also TP23.1
- net N$407: now also C20.2; no longer R51.1, R52.1
- net N$5: now also D3.A, D5.A, TP21.1, TP7.1, U$4.2; no longer R51.2, U$4.4
- net N$9: now also R45.1; no longer R49.1
- net VBUS: now also Q2.5, R39.2, R50.2
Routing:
- net N$520: track 11.8 -> 0.00 mm
- net N$503: track 11.8 -> 0.00 mm
- net N$504: track 11.7 -> 0.00 mm
- net N$528: track 11.7 -> 0.00 mm
- net N$524: track 11.6 -> 0.00 mm
- net N$500: track 7.45 -> 0.00 mm
- net N$519: track 7.44 -> 0.00 mm
- net SPARE4: track 7.08 -> 0.00 mm
- net N$525: track 5.09 -> 0.00 mm
- net AUX_VBUS1: track 2.48 -> 0.00 mm
- net AUX_VBUS2: track 2.25 -> 0.00 mm
- net AUX_!SHUTDOWN: track 1.79 -> 0.00 mm
- net AUX_GND1: track 1.72 -> 0.00 mm
- net AUX_CAN2_L: track 1.52 -> 0.00 mm
- net AUX_CAN2_H: track 1.29 -> 0.00 mm
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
